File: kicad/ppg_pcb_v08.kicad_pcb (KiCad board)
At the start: 4 copper layers, 13.5 x 13.5 mm, 37 parts, among them J1 12V, J2 GND, J3 TXP, J4 TXN, J5 RXP, J6 RXN, J7 SWDIO, J8 SWCLK, J9 NRST, U1 MAXM86161EFD+, U2 STM32C011F6U6, U3 XR33194, U4 MCP1703A-5002E/MC, U5 MCP1703A-3302E/MC, U6 XR33183

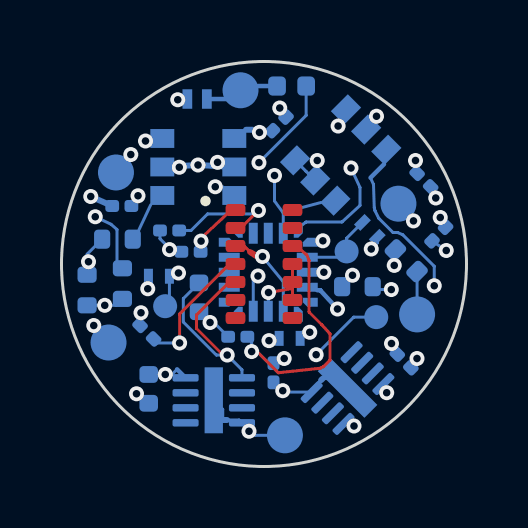
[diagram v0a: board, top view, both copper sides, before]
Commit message: Correct MCP1703A MC footprints and reroute RS-422 PCB
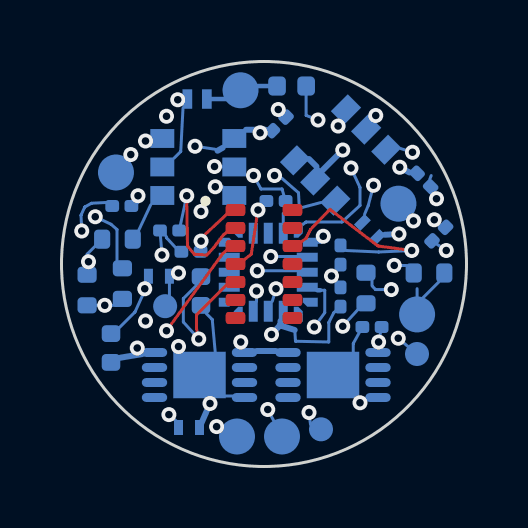
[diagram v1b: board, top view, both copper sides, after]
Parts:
- U2: footprint Package_DFN_QFN:ST_UFQFPN-20_3x3mm_P0.5mm -> SleepBud:ST_UFQFPN-20_3x3mm_P0.5mm_NoSilk
- U4, U5: footprint Package_DFN_QFN:DFN-8-1EP_2x3mm_P0.5mm_EP0.61x2.2mm -> SleepBud:MCP1703A_MC_DFN8_3x2mm_P0.5mm
- moved C4 6.14 mm to (20.4, 14.9), turned to 0 degrees
- moved J6 5.31 mm to (19.1, 22.8)
- moved D6 4.48 mm to (17.5, 22.4)
- moved C5 4.38 mm to (22.6, 16.7), turned to -90 degrees
- moved J7 4.17 mm to (21.9, 22.5)
- moved J8 4.15 mm to (25.1, 20.0)
- moved C11 3.37 mm to (22.6, 18.1), turned to 90 degrees
- moved C13 1.85 mm to (14.9, 19.8), turned to 90 degrees
- moved C14 1.56 mm to (23.6, 19.1), turned to 180 degrees
- moved U4 0.97 mm to (17.9, 20.7)
- moved R6 0.86 mm to (25.5, 17.3), turned to 0 degrees
- moved U5 0.65 mm to (22.3, 20.7), turned to 180 degrees
- moved R5 0.29 mm to (23.4, 17.8), turned to 90 degrees
- moved C1 0.22 mm to (17.9, 17.9)
- moved J2 0.11 mm to (20.6, 22.8)
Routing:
- net /TXP_DRV: track 8.72 -> 27.3 mm, vias 2 -> 4
- net /SWCLK: track 2.58 -> 11.1 mm, vias 0 -> 3
- net 5V_LED: track 14.5 -> 7.13 mm
- net /SWDIO: track 7.72 -> 14.3 mm
- net /RXN: track 3.23 -> 8.99 mm
- net /SCL: track 8.68 -> 13.4 mm
- net GND: track 17.5 -> 14.1 mm, vias 18 -> 15
- net 12V: track 14.2 -> 16.9 mm, vias 2 -> 3
- net /SDA: track 10.8 -> 13.3 mm
- net /VLDO: track 4.44 -> 1.94 mm
- net 3V3: track 35.1 -> 33.4 mm
- net /NRST: track 4.99 -> 4.25 mm
- net /VREF: track 7.34 -> 6.77 mm
